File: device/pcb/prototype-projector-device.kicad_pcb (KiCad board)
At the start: 2 copper layers, 40 x 35 mm, 22 parts, among them J1 LED, J2 Serial-UPDI, J3 UART, J4 DMX1, J5 DMX2, U1 ATtiny202-SS, U2 NJM78L33SU3, U3 CL6808, U4 MAX3485

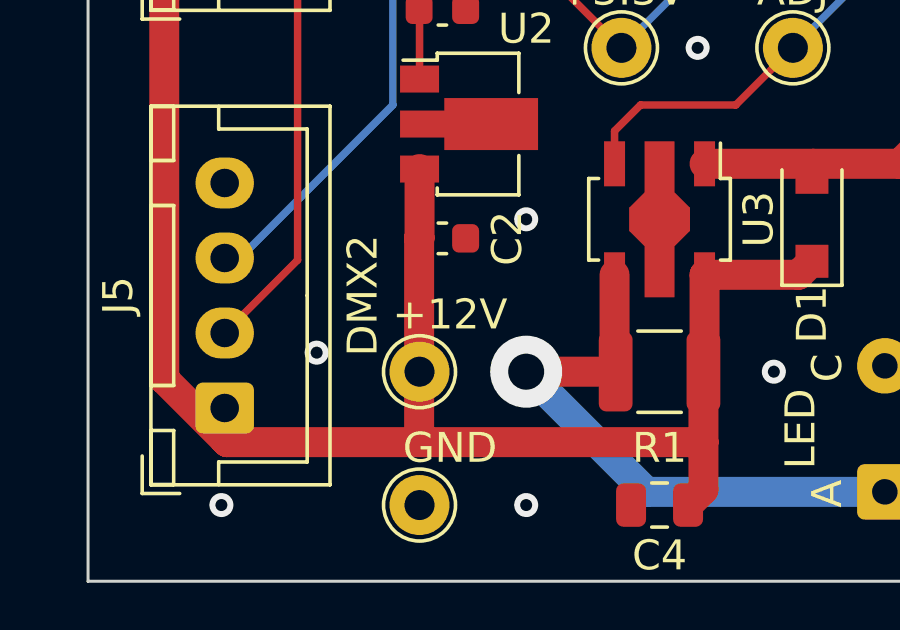
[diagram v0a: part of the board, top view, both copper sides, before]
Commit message: modify: 24V駆動対応 v0.1.1
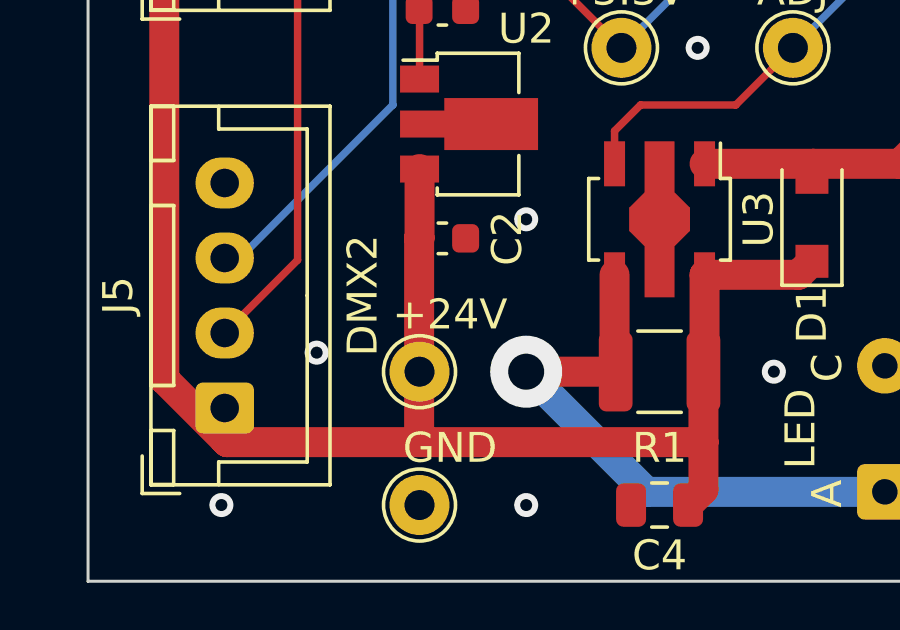
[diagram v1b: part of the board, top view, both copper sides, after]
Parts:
- C2: value 1u -> 1u50V
- TP1: value +12V -> +24V
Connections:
- net +12V renamed +24V
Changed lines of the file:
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@@
   (net 1 "+3.3V")
   (net 2 "GND")
-  (net 3 "+12V")
+  (net 3 "+24V")
   (net 4 "Net-(D1-Pad2)")
   (net 5 "Net-(D2-Pad1)")
@@
       (effects (font (size 1 1) (thickness 0.15)))
     )
-    (fp_text value "+12V" (at 1.016 -1.905) (layer "F.SilkS")
+    (fp_text value "+24V" (at 1.016 -1.905) (layer "F.SilkS")
       (effects (font (size 1 1) (thickness 0.15)))
     )
@@
     (fp_circle (center 0 0) (end 1.5 0) (layer "F.CrtYd") (width 0.05) (fill none))
     (pad "1" thru_hole circle (at 0 0) (size 2 2) (drill 1) (layers *.Cu *.Mask)
-      (net 3 "+12V") (pinfunction "1") (pintype "passive"))
+      (net 3 "+24V") (pinfunction "1") (pintype "passive"))
   )
   (footprint "Connector_PinHeader_2.54mm:PinHeader_1x03_P2.54mm_Vertical" (layer "F.Cu")
@@
       (net 7 "Net-(J1-Pad1)") (pinfunction "ISNS") (pintype "input"))
     (pad "5" smd rect (at 1.85 -1.5 270) (size 1.5 0.7) (layers "F.Cu" "F.Paste" "F.Mask")
-      (net 3 "+12V") (pinfunction "VIN") (pintype "power_in"))
+      (net 3 "+24V") (pinfunction "VIN") (pintype "power_in"))
     (model "${KICAD6_3DMODEL_DIR}/Package_TO_SOT_SMD.3dshapes/SOT-89-5.wrl"
       (offset (xyz 0 0 0))
@@
     (fp_line (start 9.95 3.4) (end 9.95 -2.35) (layer "F.Fab") (width 0.1))
     (pad "1" thru_hole roundrect (at 0 0 90) (size 1.7 1.95) (drill 0.95) (layers *.Cu *.Mask) (roundrect_rratio 0.1470588235)
-      (net 3 "+12V") (pinfunction "Pin_1") (pintype "passive"))
+      (net 3 "+24V") (pinfunction "Pin_1") (pintype "passive"))
     (pad "2" thru_hole oval (at 2.5 0 90) (size 1.7 1.95) (drill 0.95) (layers *.Cu *.Mask)
       (net 11 "Net-(J4-Pad2)") (pinfunction "Pin_2") (pintype "passive"))
@@
       (effects (font (size 1 1) (thickness 0.15)))
     )
-    (fp_text value "1u" (at 0 1.43) (layer "F.Fab")
+    (fp_text value "1u50V" (at 0 1.43) (layer "F.Fab")
       (effects (font (size 1 1) (thickness 0.15)))
     )
@@
     (fp_line (start -0.8 0.4) (end -0.8 -0.4) (layer "F.Fab") (width 0.1))
     (pad "1" smd roundrect (at -0.775 0) (size 0.9 0.95) (layers "F.Cu" "F.Paste" "F.Mask") (roundrect_rratio 0.25)
-      (net 3 "+12V") (pintype "passive"))
+      (net 3 "+24V") (pintype "passive"))
     (pad "2" smd roundrect (at 0.775 0) (size 0.9 0.95) (layers "F.Cu" "F.Paste" "F.Mask") (roundrect_rratio 0.25)
       (net 2 "GND") (pintype "passive"))
@@
     (fp_line (start 9.95 3.4) (end 9.95 -2.35) (layer "F.Fab") (width 0.1))
     (pad "1" thru_hole roundrect (at 0 0 90) (size 1.7 1.95) (drill 0.95) (layers *.Cu *.Mask) (roundrect_rratio 0.1470588235)
-      (net 3 "+12V") (pinfunction "Pin_1") (pintype "passive"))
+      (net 3 "+24V") (pinfunction "Pin_1") (pintype "passive"))
     (pad "2" thru_hole oval (at 2.5 0 90) (size 1.7 1.95) (drill 0.95) (layers *.Cu *.Mask)
       (net 11 "Net-(J4-Pad2)") (pinfunction "Pin_2") (pintype "passive"))
@@
       (net 7 "Net-(J1-Pad1)") (pintype "passive"))
     (pad "2" smd roundrect (at 1.4625 0) (size 1.125 2.65) (layers "F.Cu" "F.Paste" "F.Mask") (roundrect_rratio 0.2222222222)
-      (net 3 "+12V") (pintype "passive"))
+      (net 3 "+24V") (pintype "passive"))
     (model "${KICAD6_3DMODEL_DIR}/Resistor_SMD.3dshapes/R_1210_3225Metric.wrl"
       (offset (xyz 0 0 0))
@@
     (fp_line (start 1 0.625) (end -1 0.625) (layer "F.Fab") (width 0.1))
     (pad "1" smd roundrect (at -0.95 0 180) (size 1 1.45) (layers "F.Cu" "F.Paste" "F.Mask") (roundrect_rratio 0.25)
-      (net 3 "+12V") (pintype "passive"))
+      (net 3 "+24V") (pintype "passive"))
     (pad "2" smd roundrect (at 0.95 0 180) (size 1 1.45) (layers "F.Cu" "F.Paste" "F.Mask") (roundrect_rratio 0.25)
       (net 2 "GND") (pintype "passive"))
@@
       ))
     (pad "3" smd rect (at -1.65 1.5) (size 1.3 0.9) (layers "F.Cu" "F.Paste" "F.Mask")
-      (net 3 "+12V") (pinfunction "IN") (pintype "power_in"))
+      (net 3 "+24V") (pinfunction "IN") (pintype "power_in"))
     (model "${KICAD6_3DMODEL_DIR}/Package_TO_SOT_SMD.3dshapes/SOT-89-3.wrl"
       (offset (xyz 0 0 0))
@@
     (fp_line (start 1.4 -0.9) (end 1.4 0.9) (layer "F.Fab") (width 0.1))
     (pad "1" smd rect (at -1.4 0 90) (size 1.1 1.1) (layers "F.Cu" "F.Paste" "F.Mask")
-      (net 3 "+12V") (pinfunction "K") (pintype "passive"))
+      (net 3 "+24V") (pinfunction "K") (pintype "passive"))
     (pad "2" smd rect (at 1.4 0 90) (size 1.1 1.1) (layers "F.Cu" "F.Paste" "F.Mask")
       (net 4 "Net-(D1-Pad2)") (pinfunction "A") (pintype "passive"))
